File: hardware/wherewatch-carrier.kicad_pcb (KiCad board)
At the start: 2 copper layers, 38.6 x 26.9 mm, 32 parts, among them J1 JST_PH_S2B-PH-SM4-TB_1x02-1MP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, J3 U.FL_Hirose_U.FL-R-SMT-1_Vert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, J4 JST_PH_S2B-PH-SM4-TB_1x02-1MP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, J5 JST_PH_S2B-PH-SM4-TB_1x02-1MP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, J6 JST_SH_SM04B-SRSS-TB_1x04-1MP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, Q1 SOT-23, Q2 SOT-23, Q3 SOT-23, SW1 SW-TH_MSK12C02, SW2 SW_SPST_TL3342, U1 Val**, U2 LGA-14_3x2.5mm_P0.5mm_LayoutB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, U3 GPSM-SMD_ATGM336H-TR, U4 TQFN-16-1EP_3x3mm_P0.5mm_EP1.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

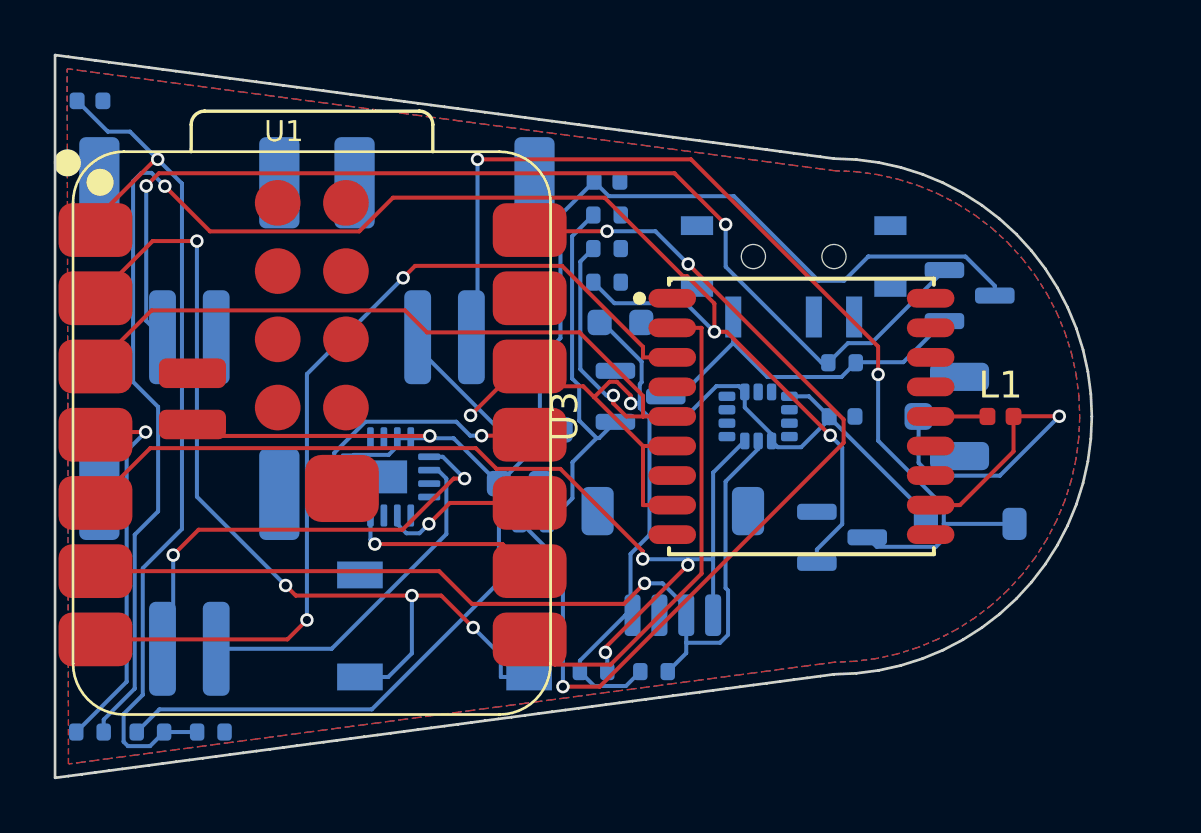
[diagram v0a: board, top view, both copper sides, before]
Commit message: hardware: route the option A carrier on 4 layers; shell lengthened so the cell clears the rounded bottom
Petrus spotted the cell poking through the case in the viewer. The cause is geometric and it was
there before this branch: a 40 mm cell inside a 43 mm shell only clears a 12 mm rounded bottom above
x = -40.5, so the cell could never sit low enough to leave the head its room. Fixed by shortening the
bottom radius to 8 mm and lengthening the pendant to 106 mm; the board outline is now derived from
those same numbers rather than a fitted line, so shell and board cannot drift apart again.

Board: head-only carrier x 14.2..51.6, 4 layers (2 plateaued at ~28 unrouted on this density, and
JLC charges little more), 286 segments, 36 vias, ground pours on the outer layers, inner layers free
for routing. Clearance 0.2 mm, track 0.15, via 0.6/0.3.

Remaining, listed in out/drc.rpt for review: 12 unconnected, 11 clearance, 8 board-edge.

Co-Authored-By: Claude Opus 5 <noreply@anthropic.com>
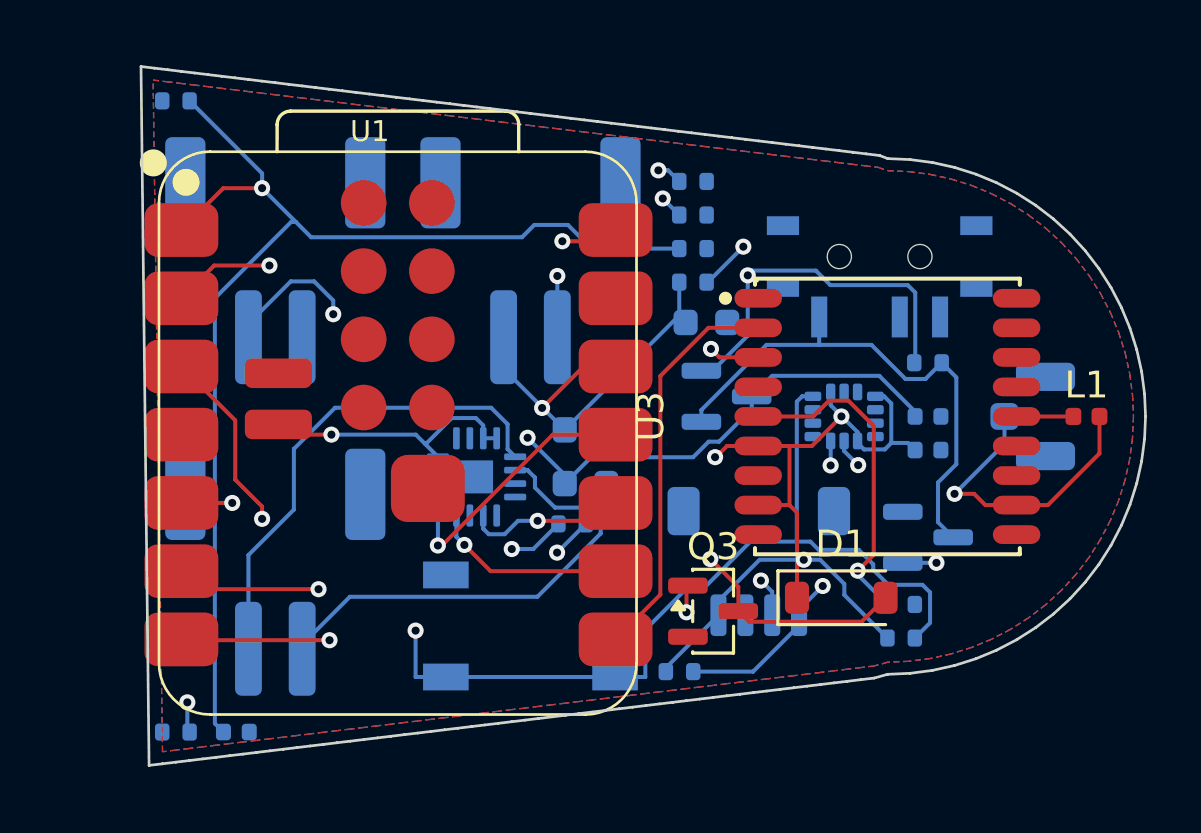
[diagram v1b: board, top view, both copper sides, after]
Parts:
- added R11: R_0402_1005Metric, R_0402_1005Metric, B.Cu at (42.5, 8.25)
- D1, Q3: moved to F.Cu
- moved R7 25.4 mm to (34.8, -6.25)
- moved C4 24.1 mm to (17.8, 11.8)
- moved R6 23.5 mm to (15.5, -11.8)
- moved R9 17.2 mm to (42.5, 7.00)
- moved C3 14.8 mm to (43.5, 0.00)
- moved R5 14.6 mm to (34.8, -5.00)
- moved Q2 11.9 mm to (43.5, 4.50)
- moved Q1 9.80 mm to (36.0, -0.75)
- moved D1 5.53 mm to (40.3, 6.75)
- moved Q3 5.53 mm to (35.5, 7.25)
- moved R8 4.06 mm to (34.8, -7.50)
- moved C5 3.44 mm to (43.5, 1.25)
- moved R10 3.44 mm to (34.8, -8.75)
- moved C6 3.20 mm to (35.2, -3.50)
- moved J3 3.20 mm to (47.9, 0.00)
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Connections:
- U2 pad 4: unconnected-(U2-INT1-Pad4) -> BTN
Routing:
- net VBAT: track 66.2 -> 35.4 mm, vias 1 -> 2
- net VBUS_DET: track 13.9 -> 38.2 mm, vias 0 -> 3
- net VIB_IN_R: track 64.1 -> 40.4 mm
- net VBUS: track 36.5 -> 16.5 mm, vias 3 -> 2
- net BTN: track 34.3 -> 52.4 mm, vias 4 -> 2
- net VIB_IN: track 14.1 -> 0.00 mm, vias 1 -> 0
- net VIB_N: track 38.4 -> 26.4 mm
- net VBAT_SENSE: track 33.5 -> 45.3 mm
- net GNSS_EN: track 32.4 -> 42.9 mm, vias 1 -> 2
- net SCL: track 35.3 -> 43.4 mm, vias 1 -> 4
- net GNSS_RX: track 34.2 -> 26.8 mm
- net BAT_RAW: track 41.1 -> 34.9 mm
- net SW_G: track 13.6 -> 19.4 mm
- net SPK_N: track 13.2 -> 17.8 mm
- net GNSS_RF: track 15.0 -> 11.4 mm
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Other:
- board size 38.6 x 26.9 mm -> 37.4 x 26 mm
- copper layers 2 -> 4

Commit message: hardware: every signal net routed; ground stitching; two resistors moved to the pads they serve
R6 and R3 had been auto-packed to the board edge, too far for the router to reach the XIAO pads they
belong to, which was the whole cause of the two unrouted nets. Pinned beside those pads and the
router closes them. 45 ground stitching vias tie the two pours together.

State: 313 track segments, 83 vias, every signal connection routed. Remaining DRC, all polish rather
than connectivity: 9 ground-pour islands, 11 clearance, 11 board-edge, 2 courtyard overlaps.
NOT ready to order until those are clean.

Co-Authored-By: Claude Opus 5 <noreply@anthropic.com>
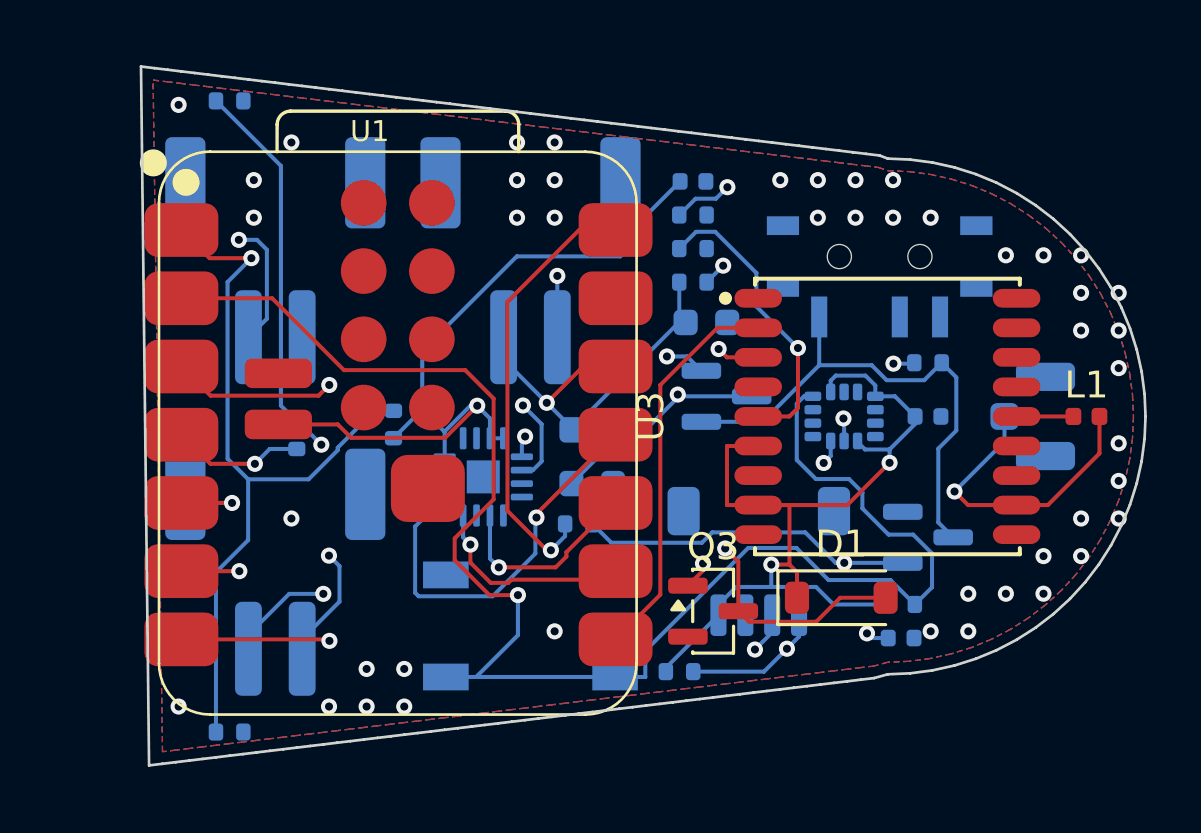
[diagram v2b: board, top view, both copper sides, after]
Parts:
- moved C4 25.0 mm to (42.5, 8.25)
- moved R7 24.9 mm to (17.5, 11.8)
- moved R8 17.8 mm to (17.5, -11.8)
- moved R9 15.4 mm to (34.8, -6.25)
- moved R6 14.5 mm to (23.6, 0.30), turned to 90 degrees
- moved C3 12.4 mm to (34.8, -8.75)
- moved R3 11.9 mm to (20.0, 0.70), turned to 90 degrees
- moved C5 1.25 mm to (43.5, 0.00)
- moved R10 1.25 mm to (34.8, -7.50)
- moved R11 1.25 mm to (42.5, 7.00)
- moved C1 0.25 mm to (31.0, 0.50)
- moved C2 0.25 mm to (31.0, 2.50)
- moved R2 0.25 mm to (30.5, 4.00)
- moved U4 0.25 mm to (26.9, 2.25)
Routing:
- net VBAT_SENSE: track 45.3 -> 61.5 mm, vias 1 -> 2
- net +3V3: track 53.9 -> 65.0 mm, vias 4 -> 3
- net VBAT: track 35.4 -> 46.0 mm
- net VIB_IN_R: track 40.4 -> 31.6 mm, vias 3 -> 2
- net BTN: track 52.4 -> 60.2 mm, vias 2 -> 1
- net VBUS_DET: track 38.2 -> 31.0 mm, vias 3 -> 2
- net VIB_IN: track 0.00 -> 4.97 mm, vias 0 -> 1
- net I2S_DIN: track 10.1 -> 14.9 mm
- net GNSS_EN: track 42.9 -> 38.9 mm
- net SPK_P: track 18.3 -> 14.7 mm, vias 0 -> 2
- net SDA: track 36.8 -> 39.5 mm
- net BAT_RAW: track 34.9 -> 33.4 mm, vias 2 -> 3
- net I2S_LRCLK: track 5.99 -> 7.51 mm
- net SPK_N: track 17.8 -> 17.0 mm, vias 0 -> 2
- net I2S_BCLK: track 7.25 -> 7.77 mm
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
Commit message: hardware: clean DRC on the carrier board (0 violations, 0 unconnected)
grok's review found 24 violations plus 9 unconnected. Four causes, all fixed in
the generator rather than the board file, since the board is regenerated:

- U2 LSM6DS3TR-C: 11 pad-to-pad complaints were the LGA-14 footprint's own
  0.15 mm pitch, not routing. Local clearance override on that footprint.
- GND stitching: margin 0.8 -> 1.3 mm, the four right-hand vias were inside
  the 0.3 mm board-edge rule.
- U1 XIAO: moved 0.7 mm in, pads 1-7 were touching the left outline.
- J1/J5 to +-7.0: the JST PH courtyard covers the wire exit and reached over
  R3 and R6, which are pinned under the XIAO pads they serve.

Ground was also split into 12 pieces, including the decoupling caps and the
IMU's own ground pads. Fixed structurally: GND pours on all four layers, and
a fanout via on every SMD ground pad placed BEFORE routing. Afterwards there
was no room, the tip fragments measured 0.22 to 0.47 mm and a via needs 0.50.

Both scripts modelled a pad as a circle of half its long side, which sits
inside the rectangle at the corners and put three vias 0.196 mm from a XIAO
pad. Replaced with true point-to-rectangle distance.

Co-Authored-By: Claude Opus 5 <noreply@anthropic.com>
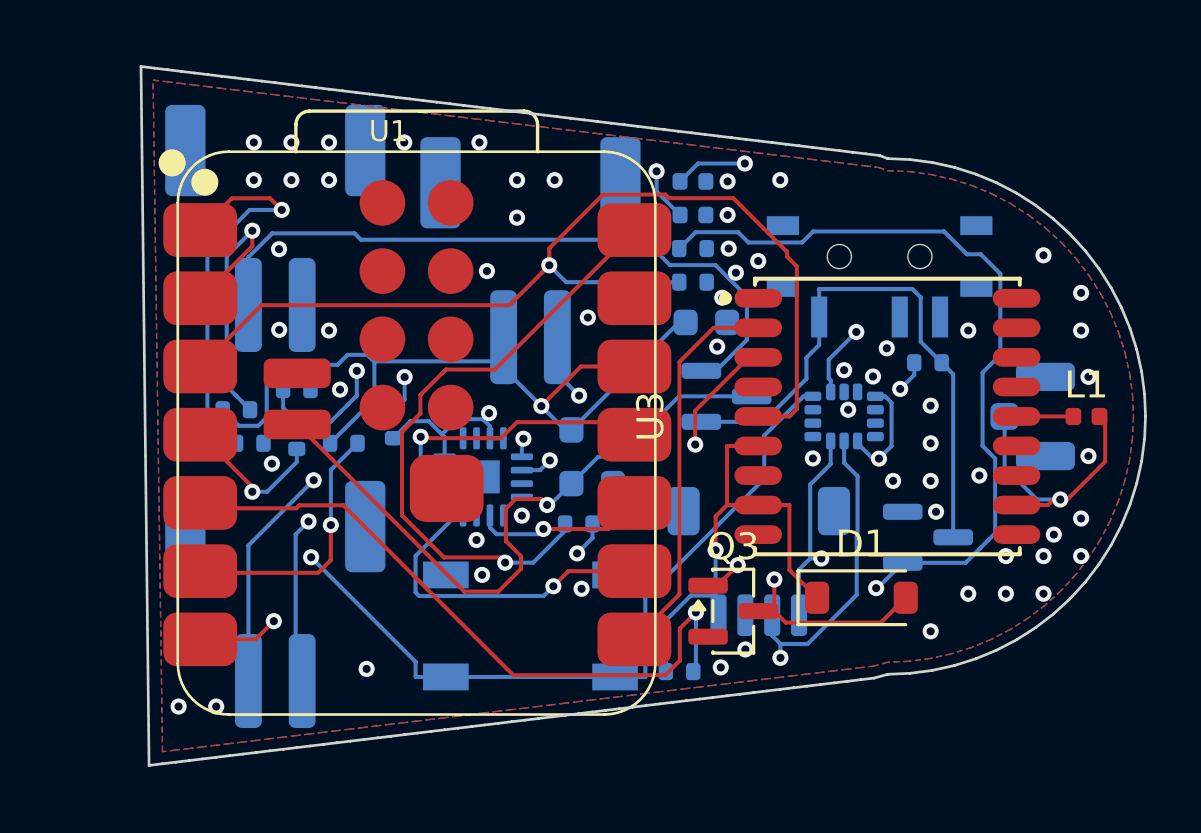
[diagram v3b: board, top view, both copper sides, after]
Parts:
- moved C4 27.5 mm to (16.0, 1.00)
- moved R11 25.8 mm to (17.8, -0.25)
- moved R5 14.3 mm to (21.8, 1.00)
- moved C5 12.4 mm to (34.8, -8.75)
- moved R8 11.0 mm to (20.0, -1.00)
- moved R7 10.8 mm to (18.2, 1.00)
- moved C3 1.25 mm to (34.8, -7.50)
- moved R10 1.25 mm to (34.8, -6.25)
- moved R9 1.25 mm to (34.8, -5.00)
- moved J1 1.20 mm to (19.2, -7.00)
- moved J5 1.20 mm to (19.2, 7.00)
- moved D1 0.75 mm to (41.0, 6.75)
- moved Q3 0.75 mm to (36.2, 7.25)
- moved U1 0.70 mm to (15.6, 11.2)
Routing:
- net VBAT_SENSE: track 61.5 -> 25.9 mm
- net +3V3: track 65.0 -> 88.2 mm, vias 3 -> 5
- net VBUS_DET: track 31.0 -> 41.8 mm
- net BTN: track 60.2 -> 51.7 mm, vias 1 -> 2
- net VIB_IN_R: track 31.6 -> 23.6 mm
- net VBUS: track 16.3 -> 22.8 mm
- net VIB_N: track 26.3 -> 19.8 mm
- net I2S_BCLK: track 7.77 -> 12.3 mm
- net VBAT: track 46.0 -> 50.0 mm, vias 2 -> 3
- net SCL: track 43.7 -> 39.9 mm, vias 4 -> 2
- net I2S_DIN: track 14.9 -> 11.3 mm
- net SPK_P: track 14.7 -> 18.2 mm
- net SW_G: track 19.3 -> 21.5 mm
- net BAT_RAW: track 33.4 -> 35.3 mm, vias 3 -> 2
- net SDA: track 39.5 -> 38.0 mm, vias 3 -> 2
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- added copper zone on In1.Cu, net GND
- added copper zone on In2.Cu, net GND

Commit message: hardware: v0.4 layout, single-sided for JLCPCB Economic assembly; DRC clean
JLCPCB's capabilities page: Economic assembly places one side only, and
Standard, the only two-sided service, needs a 70 x 70 mm board. So every
JLC-placed part now sits on the bottom (30 parts, 12 Basic + 8 Extended
lines) and the top carries only the two hand-soldered castellated modules
(U1 XIAO, U3 ATGM336H) and J6.

- L1, Q3, D1 moved to the bottom; the packer is bottom-only.
- J6 becomes four 1.0 mm solder pads on the top (new footprint
  lib/WhereWatch.pretty/OLED_Pads_1x04_P1.00mm, courtyard = pads + 0.25):
  the bottom had no room for the moved parts with the SH connector, and
  the screen is DNP for the first five anyway.
- Routed with freerouting 1.9.0; all signal nets complete without
  close_nets.py. stitch_gnd.py now respects footprint keepouts (J3).
- DRC errors: 0 violations, 0 unconnected. 328 tracks, 113 vias.
- Order files: gerbers-single.zip, bom-jlc.csv, cpl-jlc-bottom.csv.
  Full BOM: sides updated, J6 DNP, U1/U3 HAND. JLC parts for 5 boards
  USD 20.71 (U3 now bought separately).

Co-Authored-By: Claude Fable 5.1 <noreply@anthropic.com>
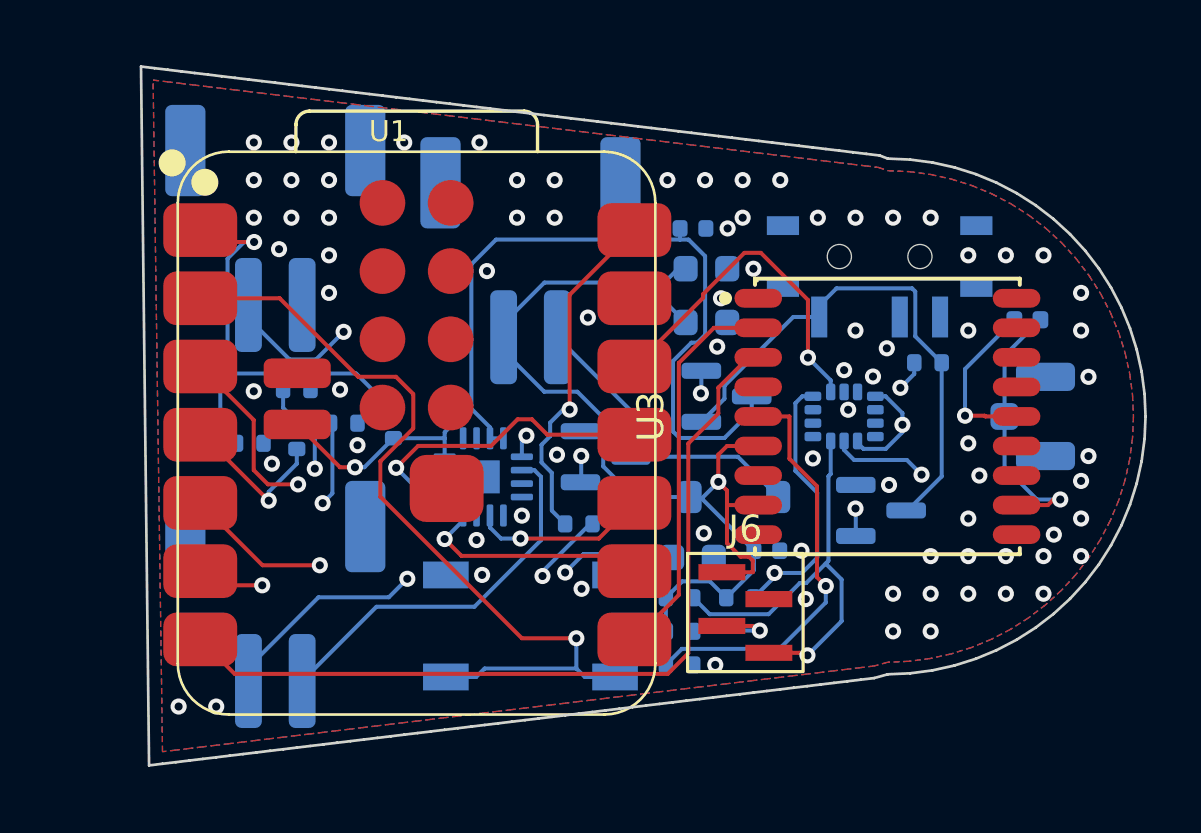
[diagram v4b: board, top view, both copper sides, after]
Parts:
- D1, L1, Q3: moved to B.Cu
- J6: value JST_SH_SM04B-SRSS-TB_1x04-1MP_P1.00mm_Horizontal -> PinHeader_1x04_P1.00mm_Vertical_SMD_Pin1Left; footprint JST_SH_SM04B-SRSS-TB_1x04-1MP_P1.00mm_Horizontal -> OLED_Pads_1x04_P1.00mm; moved to F.Cu
- moved R11 20.0 mm to (36.5, 6.75)
- moved R10 14.5 mm to (21.8, 0.25)
- moved R5 14.3 mm to (34.2, 8.00)
- moved R9 14.3 mm to (34.2, 9.25)
- moved C5 14.0 mm to (37.5, 5.00)
- moved Q3 7.46 mm to (31.5, 1.50)
- moved D1 6.05 mm to (36.3, 3.00)
- moved C1 5.84 mm to (35.2, -3.50)
- moved C2 4.65 mm to (34.8, 5.25)
- moved L1 4.22 mm to (47.2, -3.60)
- moved R4 2.75 mm to (34.2, 6.75)
- moved Q2 2.02 mm to (41.8, 3.50)
- moved C6 2.00 mm to (35.2, -5.50)
- moved J6 1.96 mm to (36.7, 7.30)
- moved C3 0.50 mm to (34.8, -7.00)
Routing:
- net +3V3: track 88.2 -> 67.2 mm, vias 5 -> 3
- net VBUS_DET: track 41.8 -> 29.0 mm, vias 2 -> 3
- net VBUS: track 22.8 -> 12.9 mm
- net VIB_N: track 19.8 -> 11.7 mm, vias 2 -> 0
- net VIB_IN_R: track 23.6 -> 15.9 mm
- net GNSS_EN: track 38.4 -> 46.0 mm, vias 1 -> 2
- net VBAT_SENSE: track 25.9 -> 19.3 mm, vias 2 -> 1
- net BAT_RAW: track 35.3 -> 28.9 mm, vias 2 -> 3
- net GNSS_RX: track 25.9 -> 31.3 mm, vias 2 -> 0
- net VCC_RF: track 2.12 -> 6.26 mm, vias 0 -> 1
- net I2S_BCLK: track 12.3 -> 8.72 mm
- net SDA: track 38.0 -> 41.2 mm
- net SPK_N: track 17.4 -> 14.2 mm, vias 2 -> 0
- net BTN: track 51.7 -> 49.2 mm
- net SPK_P: track 18.2 -> 15.9 mm
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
